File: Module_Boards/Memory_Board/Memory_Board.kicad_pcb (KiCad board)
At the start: 6 copper layers, 10.8 x 15.2 mm, 17 parts, among them U1 MX25U12832FZNI02-TR, U2 MX25U25643GZ4I00-T

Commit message: Big push. Fixed the issues that were pending. See github
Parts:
- added kibuzzard-6743EB85: G***, kibuzzard-6743EB85, F.Cu at (148.1, 100.2)
- added kibuzzard-6743EB8D: G***, kibuzzard-6743EB8D, F.Cu at (154.7, 100.2)
- moved R7 11.8 mm to (156.5, 100.2), turned to 180 degrees
- moved kibuzzard-672506D5 11.7 mm to (157.9, 95.4), turned to -90 degrees
- moved R8 10.0 mm to (154.6, 90.5), turned to 0 degrees
- moved C1 8.58 mm to (146.2, 90.6), turned to 180 degrees
- moved C2 8.41 mm to (152.8, 90.5), turned to 180 degrees
- moved R1 8.20 mm to (146.2, 100.2), turned to 0 degrees
- moved R5 8.02 mm to (152.8, 100.2), turned to 0 degrees
- moved U2 7.89 mm to (155.2, 95.4), turned to 90 degrees
- moved G*** 7.71 mm to (155.1, 95.4), turned to -90 degrees
- moved R4 7.42 mm to (148.0, 90.5), turned to 0 degrees
- moved R2 7.08 mm to (149.9, 90.5), turned to 180 degrees
- moved R3 6.61 mm to (149.9, 100.2), turned to 180 degrees
- moved G*** 4.18 mm to (146.7, 95.7), turned to -90 degrees
- moved J1 3.19 mm to (151.9, 95.4), turned to 180 degrees
- moved kibuzzard-672506E3 2.37 mm to (151.3, 95.7), turned to -90 degrees
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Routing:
- net FLASH_CLK: track 24.1 -> 21.9 mm
- net FLASH_MOSI_(IO0): track 22.9 -> 23.6 mm, vias 2 -> 3
- added copper zone on In4.Cu, net GND
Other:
- board size 10.8 x 15.2 mm -> 15.2 x 10.8 mm
- board text added: "#"
- board text added: "1V8"
- board text added: "CLK"
- board text added: "CS1"
- board text added: "CS2"
- board text added: "GND"
- board text added: "MI"
- board text added: "MO"
- board text added: "RE1"
- board text added: "RE2"
- board text added: "WP1"
- board text added: "WP2"

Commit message: Final revision and production files
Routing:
- net ~{FLASH_1_CS}: track 6.46 -> 7.10 mm
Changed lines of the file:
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@@
+	)
+	(segment
+		(start 146.6325 97.6325)
+		(end 146.6325 98.085)
+		(width 0.12)
+		(layer "F.Cu")
+		(net 3)
+	)
+	(segment
+		(start 144.2625 94.75)
+		(end 145.35 94.75)
+		(width 0.12)
+		(layer "F.Cu")
+		(net 3)
 	)
 	(segment
@@
 		(end 146.6325 99.135)
 		(width 0.5)
+		(layer "F.Cu")
+		(net 3)
+	)
+	(segment
+		(start 145.7625 96.7625)
+		(end 146.6325 97.6325)
+		(width 0.12)
 		(layer "F.Cu")
 		(net 3)
@@
 	)
 	(segment
-		(start 146.6325 97.6325)
-		(end 146.6325 98.085)
+		(start 145.7625 95.1625)
+		(end 145.7625 96.7625)
 		(width 0.12)
 		(layer "F.Cu")
@@
 	)
 	(segment
-		(start 145.7625 96.7625)
-		(end 146.6325 97.6325)
+		(start 145.35 94.75)
+		(end 145.7625 95.1625)
 		(width 0.12)
 		(layer "F.Cu")
@@
 		(width 0.12)
 		(layer "F.Cu")
-		(net 3)
-	)
-	(segment
-		(start 145.7625 96.25)
-		(end 145.7625 96.7625)
-		(width 0.12)
-		(layer "F.Cu")
-		(net 3)
-	)
-	(segment
-		(start 144.2625 94.75)
-		(end 145.7625 96.25)
-		(width 0.12)
-		(layer "F.Cu")

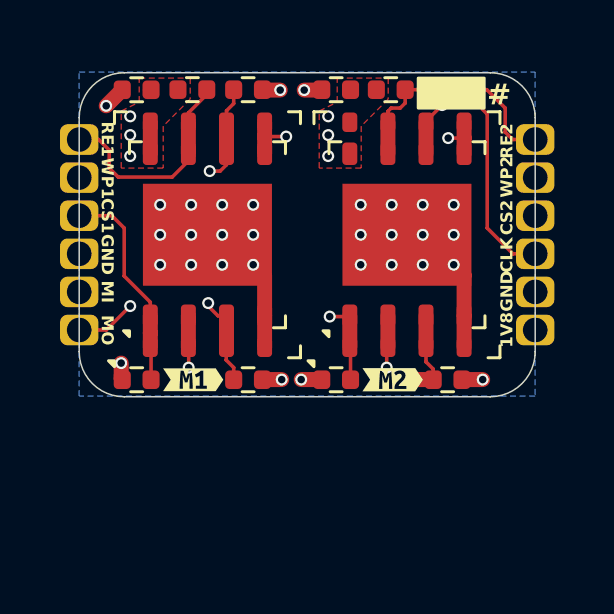
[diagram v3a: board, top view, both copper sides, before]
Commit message: Added fabrication panel. Now with latest designs
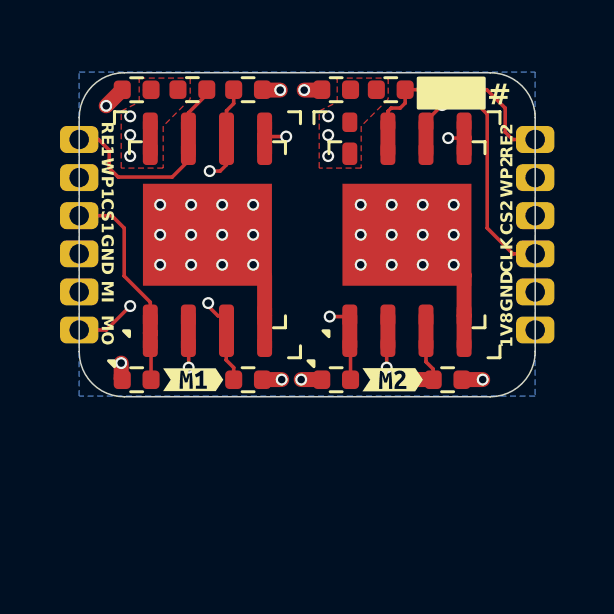
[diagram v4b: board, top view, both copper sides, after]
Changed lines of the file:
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@@
+			)
+		)
+		(property "MPN" "CRCW040210K0FKEDHP"
+			(at 0 0 180)
+			(unlocked yes)
+			(layer "F.Fab")
+			(hide yes)
+			(effects
+				(font
+					(size 1 1)
+					(thickness 0.15)
+				)
 			)
 		)
@@
 		(property "Description" "Thick Film Resistors - SMD 0.2W 10Kohms 1% High Power AEC-Q200"
 			(at 0 -9 0)
+			(unlocked yes)
+			(layer "F.Fab")
+			(hide yes)
+			(effects
+				(font
+					(size 1 1)
+					(thickness 0.15)
+				)
+			)
+		)
+		(property "MPN" "CRCW040210K0FKEDHP"
+			(at 0 0 0)
 			(unlocked yes)
 			(layer "F.Fab")
@@
 			)
 		)
+		(property "MPN" "CRCW040210K0FKEDHP"
+			(at 0 0 0)
+			(unlocked yes)
+			(layer "F.Fab")
+			(hide yes)
+			(effects
+				(font
+					(size 1 1)
+					(thickness 0.15)
+				)
+			)
+		)
 		(sheetname "Root")
 		(sheetfile "Memory_Board.kicad_sch")
@@
 			)
 		)
+		(property "MPN" "CRCW040210K0FKEDHP"
+			(at 0 0 0)
+			(unlocked yes)
+			(layer "F.Fab")
+			(hide yes)
+			(effects
+				(font
+					(size 1 1)
+					(thickness 0.15)
+				)
+			)
+		)
 		(sheetname "Root")
 		(sheetfile "Memory_Board.kicad_sch")
@@
 		(sheetname "Root")
 		(sheetfile "Memory_Board.kicad_sch")
-		(attr smd)
+		(attr smd exclude_from_bom)
 		(fp_rect
 			(start -7.6 -5.4)
@@
 		(pad "1" thru_hole roundrect
 			(at -7.6 -3.175 270)
-			(size 1.02 1.28)
-			(drill 0.82)
+			(size 0.9 1.28)
+			(drill 0.65)
 			(property pad_prop_castellated)
 			(layers "*.Cu" "*.Mask")
@@
 		(pad "2" thru_hole roundrect
 			(at -7.6 -1.905 270)
-			(size 1.02 1.28)
-			(drill 0.82)
+			(size 0.9 1.28)
+			(drill 0.65)
 			(property pad_prop_castellated)
 			(layers "*.Cu" "*.Mask")
@@
 		(pad "3" thru_hole roundrect
 			(at -7.6 -0.635 270)
-			(size 1.02 1.28)
-			(drill 0.82)
+			(size 0.9 1.28)
+			(drill 0.65)
 			(property pad_prop_castellated)
 			(layers "*.Cu" "*.Mask")
@@
 		(pad "4" thru_hole roundrect
 			(at -7.6 0.635 270)
-			(size 1.02 1.28)
-			(drill 0.82)
+			(size 0.9 1.28)
+			(drill 0.65)
 			(property pad_prop_castellated)
 			(layers "*.Cu" "*.Mask")
@@
 		(pad "5" thru_hole roundrect
 			(at -7.6 1.905 270)
-			(size 1.02 1.28)
-			(drill 0.82)
+			(size 0.9 1.28)
+			(drill 0.65)
 			(property pad_prop_castellated)
 			(layers "*.Cu" "*.Mask")
@@
 		(pad "6" thru_hole roundrect
 			(at -7.6 3.175 270)
-			(size 1.02 1.28)
-			(drill 0.82)
+			(size 0.9 1.28)
+			(drill 0.65)
 			(property pad_prop_castellated)
 			(layers "*.Cu" "*.Mask")
@@
 		(pad "7" thru_hole roundrect
 			(at 7.6 3.175 270)
-			(size 1.02 1.28)
-			(drill 0.82)
+			(size 0.9 1.28)
+			(drill 0.65)
 			(property pad_prop_castellated)
 			(layers "*.Cu" "*.Mask")
@@
 		(pad "8" thru_hole roundrect
 			(at 7.6 1.905 270)
-			(size 1.02 1.28)
-			(drill 0.82)
+			(size 0.9 1.28)
+			(drill 0.65)
 			(property pad_prop_castellated)
 			(layers "*.Cu" "*.Mask")
@@
 		(pad "9" thru_hole roundrect
 			(at 7.6 0.635 270)
-			(size 1.02 1.28)
-			(drill 0.82)
+			(size 0.9 1.28)
+			(drill 0.65)
 			(property pad_prop_castellated)
 			(layers "*.Cu" "*.Mask")
@@
 		(pad "10" thru_hole roundrect
 			(at 7.6 -0.635 270)
-			(size 1.02 1.28)
-			(drill 0.82)
+			(size 0.9 1.28)
+			(drill 0.65)
 			(property pad_prop_castellated)
 			(layers "*.Cu" "*.Mask")
@@
 		(pad "11" thru_hole roundrect
 			(at 7.6 -1.905 270)
-			(size 1.02 1.28)
-			(drill 0.82)
+			(size 0.9 1.28)
+			(drill 0.65)
 			(property pad_prop_castellated)
 			(layers "*.Cu" "*.Mask")
@@
 		(pad "12" thru_hole roundrect
 			(at 7.6 -3.175 270)
-			(size 1.02 1.28)
-			(drill 0.82)
+			(size 0.9 1.28)
+			(drill 0.65)
 			(property pad_prop_castellated)
 			(layers "*.Cu" "*.Mask")
@@
 		(property "Description" "Thick Film Resistors - SMD 0.2W 10Kohms 1% High Power AEC-Q200"
 			(at 0 -9 0)
+			(unlocked yes)
+			(layer "F.Fab")
+			(hide yes)
+			(effects
+				(font
+					(size 1 1)
+					(thickness 0.15)
+				)
+			)
+		)
+		(property "MPN" "CRCW040210K0FKEDHP"
+			(at 0 0 0)
 			(unlocked yes)
 			(layer "F.Fab")
@@
 			)
 		)
+		(property "MPN" "CRCW040210K0FKEDHP"
+			(at 0 0 180)
+			(unlocked yes)
+			(layer "F.Fab")
+			(hide yes)
+			(effects
+				(font
+					(size 1 1)
+					(thickness 0.15)
+				)
+			)
+		)
 		(sheetname "Root")
 		(sheetfile "Memory_Board.kicad_sch")
@@
 			(unlocked yes)
 			(layer "F.Fab")
+			(hide yes)
+			(effects
+				(font
+					(size 1 1)
+					(thickness 0.15)
+				)
+			)
+		)
+		(property "MPN" "CRCW040210K0FKEDHP"
+			(at 0 0 180)
+			(unlocked yes)
+			(layer "F.Fab")
